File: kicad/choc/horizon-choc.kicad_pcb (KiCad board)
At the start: 2 copper layers, 252 x 68 mm, 115 parts, among them SW1 SW_Push, SW10 SW_Push, SW11 SW_Push, SW12 SW_Push, SW13 SW_Push, SW14 SW_Push, SW15 SW_Push, SW16 SW_Push, SW17 SW_Push, SW18 SW_Push, SW19 SW_Push, SW2 SW_Push, SW20 SW_Push, SW21 SW_Push, SW22 SW_Push, SW23 SW_Push, SW24 SW_Push, SW25 SW_Push, SW26 SW_Push, SW27 SW_Push, SW28 SW_Push, SW29 SW_Push, SW3 SW_Push, SW30 SW_Push, SW31 SW_Push, SW32 SW_Push, SW33 SW_Push, SW34 SW_Push, SW35 SW_Push, SW36 SW_Push, SW37 SW_Push, SW38 SW_Push, SW39 SW_Push, SW4 SW_Push, SW40 SW_Push, SW41 SW_Push, SW42 SW_Push, SW43 SW_Push, SW44 SW_Push, SW45 SW_Push, SW46 SW_Push, SW47 SW_Push, SW48 SW_Push, SW49 SW_Push, SW5 SW_Push, SW50 SW_Push, SW51 SW_Push, SW52 SW_Push, SW6 SW_Push, SW7 SW_Push, SW8 SW_Push, SW9 SW_Push, U1 PRO-MICRO

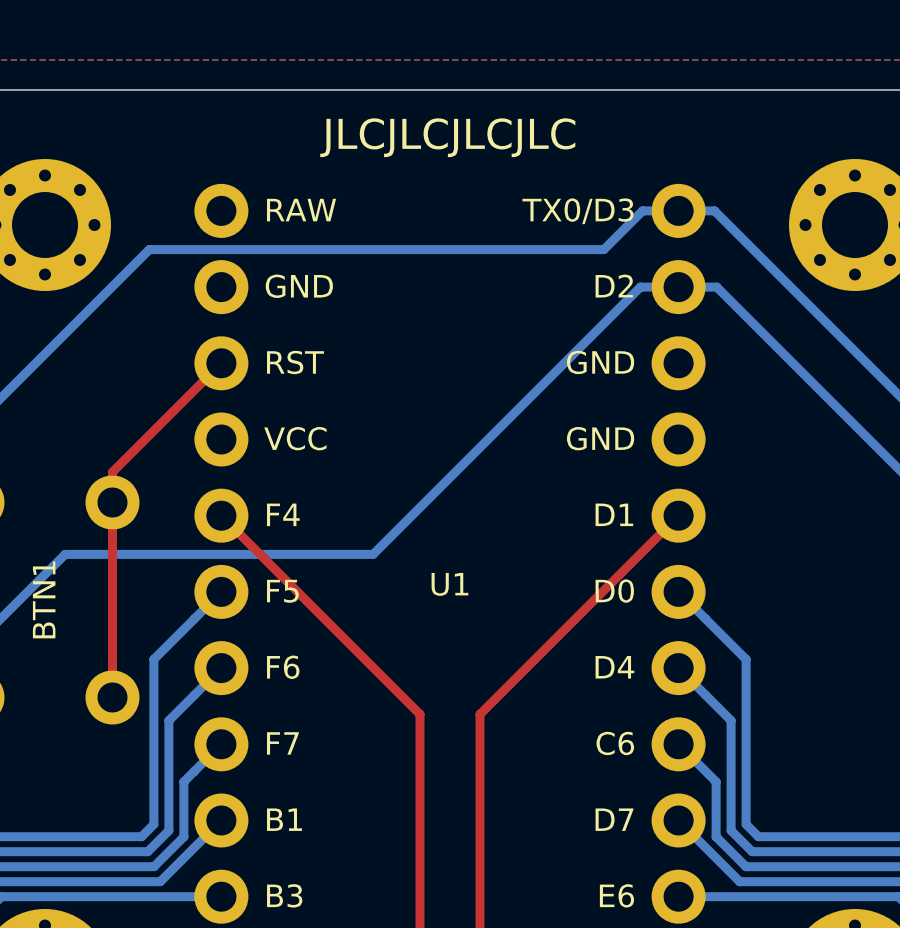
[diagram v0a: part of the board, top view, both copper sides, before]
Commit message: Preserve logos on plate PCBs
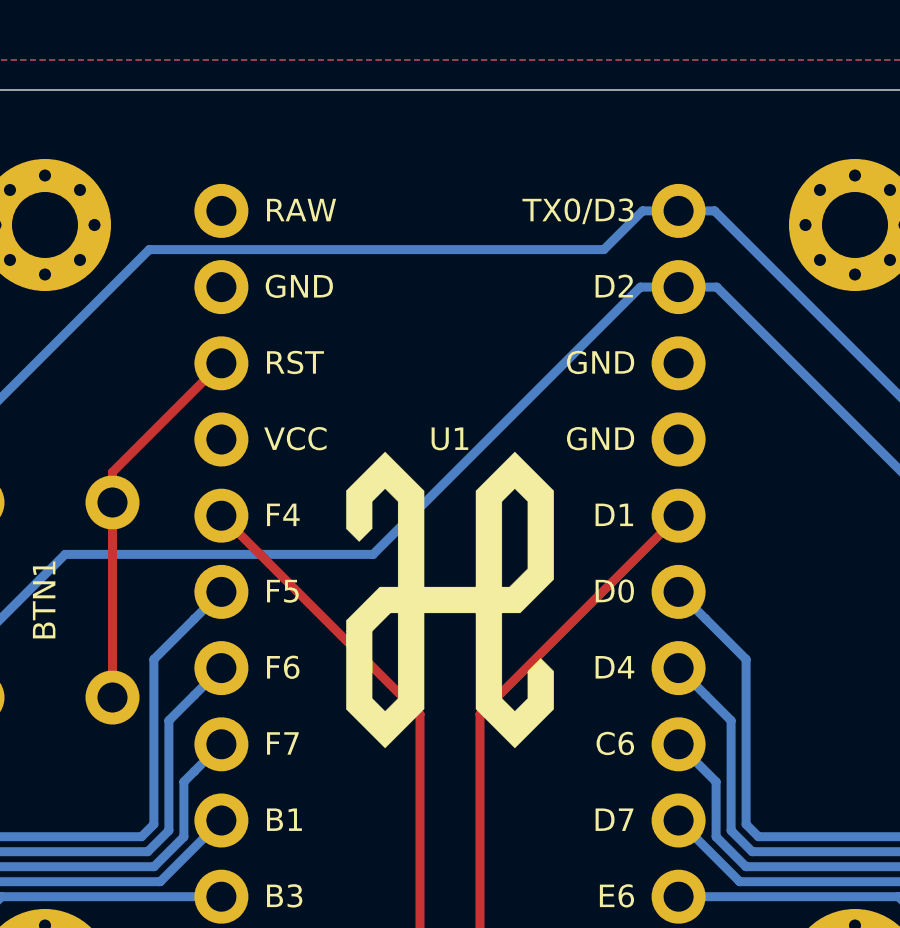
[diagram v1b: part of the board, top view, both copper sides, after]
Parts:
- added LOGO2: Logo-Top, horizon-footprints:Logo_Horizon_H, F.Cu at (202.0, 112.0)
- LOGO1: value Logo -> Logo-Bottom
- moved LOGO1 23.0 mm to (202.0, 100.5)
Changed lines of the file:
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@@
     (tracks 518)
     (zones 0)
-    (modules 115)
+    (modules 116)
     (nets 81)
   )
@@
     (add_net "Net-(H7-Pad1)")
     (add_net "Net-(H8-Pad1)")
+    (add_net "Net-(U1-Pad24)")
     (add_net RESET)
     (add_net ROW1)
@@
     (add_net ROW3)
     (add_net ROW4)
+    (add_net VCC)
   )
   (net_class Power ""
@@
     (add_net GND)
   )
+  (module horizon-footprints:Logo_Horizon_H (layer F.Cu)
+    (at 202 112)
+    (fp_text reference LOGO2 (at 0 2) (layer F.SilkS) hide
+      (effects (font (size 1.524 1.524) (thickness 0.3)))
+    )
+    (fp_text value Logo-Top (at 0 -2) (layer F.SilkS) hide
+      (effects (font (size 1.524 1.524) (thickness 0.3)))
+    )
+    (fp_poly (pts (xy 2.811161 -4.287795) (xy 3.459892 -3.639066) (xy 3.459892 -0.685799) (xy 2.900748 -0.126656)
+      (xy 2.341604 0.432486) (xy 1.731319 0.432486) (xy 1.731319 3.280722) (xy 1.94722 3.49662)
+      (xy 2.163122 3.712519) (xy 2.37902 3.496617) (xy 2.594919 3.280715) (xy 2.594919 2.378679)
+      (xy 2.810817 2.162777) (xy 2.83116 2.14244) (xy 2.850995 2.122623) (xy 2.870235 2.103411)
+      (xy 2.888793 2.084893) (xy 2.906579 2.067156) (xy 2.923508 2.050287) (xy 2.93949 2.034374)
+      (xy 2.954438 2.019503) (xy 2.968264 2.005761) (xy 2.980881 1.993237) (xy 2.9922 1.982017)
+      (xy 3.002134 1.972189) (xy 3.010594 1.96384) (xy 3.017494 1.957056) (xy 3.022745 1.951926)
+      (xy 3.02626 1.948537) (xy 3.02795 1.946975) (xy 3.028092 1.946875) (xy 3.029178 1.947832)
+      (xy 3.032118 1.950645) (xy 3.036821 1.955226) (xy 3.043201 1.961488) (xy 3.051169 1.969343)
+      (xy 3.060638 1.978705) (xy 3.07152 1.989485) (xy 3.083726 2.001596) (xy 3.097169 2.014952)
+      (xy 3.111761 2.029464) (xy 3.127413 2.045045) (xy 3.144038 2.061608) (xy 3.161548 2.079065)
+      (xy 3.179855 2.097329) (xy 3.198872 2.116313) (xy 3.218509 2.135929) (xy 3.238679 2.15609)
+      (xy 3.24468 2.162091) (xy 3.459892 2.377306) (xy 3.459892 3.639066) (xy 2.16243 4.936524)
+      (xy 1.513702 4.287791) (xy 0.864973 3.639058) (xy 0.864973 0.432486) (xy -0.8636 0.432486)
+      (xy -0.8636 3.639058) (xy -1.511985 4.287448) (xy -1.547393 4.322855) (xy -1.582321 4.357781)
+      (xy -1.616719 4.392174) (xy -1.650537 4.425985) (xy -1.683724 4.459163) (xy -1.716229 4.491659)
+      (xy -1.748003 4.52342) (xy -1.778995 4.554399) (xy -1.809155 4.584543) (xy -1.838431 4.613803)
+      (xy -1.866775 4.642128) (xy -1.894136 4.669469) (xy -1.920462 4.695774) (xy -1.945705 4.720994)
+      (xy -1.969813 4.745078) (xy -1.992736 4.767976) (xy -2.014425 4.789637) (xy -2.034827 4.810012)
+      (xy -2.053894 4.82905) (xy -2.071574 4.8467) (xy -2.087818 4.862913) (xy -2.102575 4.877638)
+      (xy -2.115795 4.890825) (xy -2.127427 4.902423) (xy -2.13742 4.912383) (xy -2.145726 4.920653)
+      (xy -2.152293 4.927184) (xy -2.15707 4.931925) (xy -2.160008 4.934826) (xy -2.161057 4.935837)
+      (xy -2.161058 4.935838) (xy -2.162058 4.934875) (xy -2.16495 4.932021) (xy -2.169682 4.927325)
+      (xy -2.176204 4.920839) (xy -2.184467 4.912612) (xy -2.194419 4.902694) (xy -2.20601 4.891136)
+      (xy -2.21919 4.877989) (xy -2.233909 4.863302) (xy -2.250116 4.847126) (xy -2.267761 4.829511)
+      (xy -2.286794 4.810508) (xy -2.307164 4.790166) (xy -2.32882 4.768536) (xy -2.351713 4.745669)
+      (xy -2.375792 4.721614) (xy -2.401007 4.696422) (xy -2.427307 4.670144) (xy -2.454642 4.642829)
+      (xy -2.482962 4.614527) (xy -2.512216 4.585291) (xy -2.542354 4.555168) (xy -2.573326 4.52421)
+      (xy -2.605081 4.492468) (xy -2.637569 4.45999) (xy -2.670739 4.426829) (xy -2.704541 4.393033)
+      (xy -2.738926 4.358654) (xy -2.773842 4.323741) (xy -2.810133 4.28745) (xy -3.458519 3.639063)
+      (xy -3.458519 1.044143) (xy -2.593546 1.044143) (xy -2.593546 3.280715) (xy -2.377648 3.496617)
+      (xy -2.161749 3.712519) (xy -1.945848 3.49662) (xy -1.729946 3.280722) (xy -1.729946 0.432486)
+      (xy -1.981884 0.432486) (xy -2.287715 0.738315) (xy -2.593546 1.044143) (xy -3.458519 1.044143)
+      (xy -3.458519 0.685798) (xy -2.899375 0.126656) (xy -2.340231 -0.432487) (xy -1.729946 -0.432487)
+      (xy -1.729946 -3.280722) (xy -1.945848 -3.496621) (xy -2.161749 -3.712519) (xy -2.377648 -3.496618)
+      (xy -2.593546 -3.280716) (xy -2.593546 -2.378679) (xy -2.809445 -2.162778) (xy -2.829787 -2.142441)
+      (xy -2.849622 -2.122623) (xy -2.868863 -2.103412) (xy -2.88742 -2.084894) (xy -2.905207 -2.067157)
+      (xy -2.922135 -2.050288) (xy -2.938117 -2.034374) (xy -2.953065 -2.019503) (xy -2.966892 -2.005762)
+      (xy -2.979508 -1.993238) (xy -2.990827 -1.982018) (xy -3.000761 -1.97219) (xy -3.009222 -1.96384)
+      (xy -3.016122 -1.957057) (xy -3.021373 -1.951927) (xy -3.024887 -1.948537) (xy -3.026578 -1.946975)
+      (xy -3.026719 -1.946876) (xy -3.027806 -1.947833) (xy -3.030745 -1.950646) (xy -3.035449 -1.955227)
+      (xy -3.041829 -1.961488) (xy -3.049797 -1.969344) (xy -3.059266 -1.978705) (xy -3.070147 -1.989485)
+      (xy -3.082354 -2.001597) (xy -3.095797 -2.014952) (xy -3.110388 -2.029464) (xy -3.126041 -2.045045)
+      (xy -3.142666 -2.061608) (xy -3.160176 -2.079066) (xy -3.178483 -2.09733) (xy -3.197499 -2.116314)
+      (xy -3.217136 -2.13593) (xy -3.237306 -2.156091) (xy -3.243307 -2.162091) (xy -3.458519 -2.377306)
+      (xy -3.458519 -3.639066) (xy -2.809789 -4.287795) (xy -2.161058 -4.936525) (xy -0.8636 -3.639059)
+      (xy -0.8636 -0.432487) (xy 0.864973 -0.432487) (xy 0.864973 -3.280716) (xy 1.731319 -3.280716)
+      (xy 1.731319 -0.432487) (xy 1.983257 -0.432487) (xy 2.289088 -0.738315) (xy 2.594919 -1.044144)
+      (xy 2.594919 -3.280722) (xy 2.379017 -3.496621) (xy 2.163115 -3.712519) (xy 1.947217 -3.496618)
+      (xy 1.731319 -3.280716) (xy 0.864973 -3.280716) (xy 0.864973 -3.639059) (xy 1.513702 -4.287792)
+      (xy 2.16243 -4.936525) (xy 2.811161 -4.287795)) (layer F.SilkS) (width 0.01))
+  )
   (module horizon-footprints:Logo_Horizon_Small (layer B.Cu)
-    (at 202 123.5 180)
-    (fp_text reference LOGO1 (at 0 0) (layer B.SilkS) hide
+    (at 202 100.5 180)
+    (fp_text reference LOGO1 (at 0 -2) (layer B.SilkS) hide
       (effects (font (size 1.524 1.524) (thickness 0.3)) (justify mirror))
     )
-    (fp_text value Logo (at 0.75 0) (layer B.SilkS) hide
+    (fp_text value Logo-Bottom (at -0.1 1) (layer B.SilkS) hide
       (effects (font (size 1.524 1.524) (thickness 0.3)) (justify mirror))
     )
@@
     (descr "SparkFun Arduino Pro Micro ATmega32U4")
     (tags "Arduino, Pro Micro")
-    (fp_text reference U1 (at 0 16.5) (layer F.SilkS)
+    (fp_text reference U1 (at 0 11.65) (layer F.SilkS)
       (effects (font (size 0.75 0.75) (thickness 0.15)))
     )
-    (fp_text value PRO-MICRO (at 0 18) (layer F.SilkS) hide
+    (fp_text value PRO-MICRO (at 0 13.65) (layer F.SilkS) hide
       (effects (font (size 0.75 0.75) (thickness 0.15)))
     )
@@
   (gr_line (start 328 161) (end 328 97) (layer B.Adhes) (width 0.05))
   (gr_line (start 78 163) (end 326 163) (layer B.Adhes) (width 0.05))
-  (gr_text "rev2 | Choc" (at 202 127.5) (layer B.SilkS)
+  (gr_text "rev2 | Choc" (at 202 104.5) (layer B.SilkS)
     (effects (font (size 1 1) (thickness 0.15)) (justify mirror))
   )
@@
   (gr_arc (start 326 161) (end 326 163) (angle -90) (layer Edge.Cuts) (width 0.05))
   (gr_line (start 328 97) (end 328 161) (layer Edge.Cuts) (width 0.05))
-  (gr_text JLCJLCJLCJLC (at 202 96.5) (layer F.SilkS)
-    (effects (font (size 1 1) (thickness 0.15)))
+  (gr_text JLCJLCJLCJLC (at 202 106.5) (layer B.SilkS)
+    (effects (font (size 1 1) (thickness 0.15)) (justify mirror))
   )
-  (gr_text github.com/skarrmann/horizon (at 202 129.5) (layer B.SilkS)
+  (gr_text github.com/skarrmann/horizon (at 202 96.5) (layer B.SilkS)
     (effects (font (size 1 1) (thickness 0.15)) (justify mirror))
   )

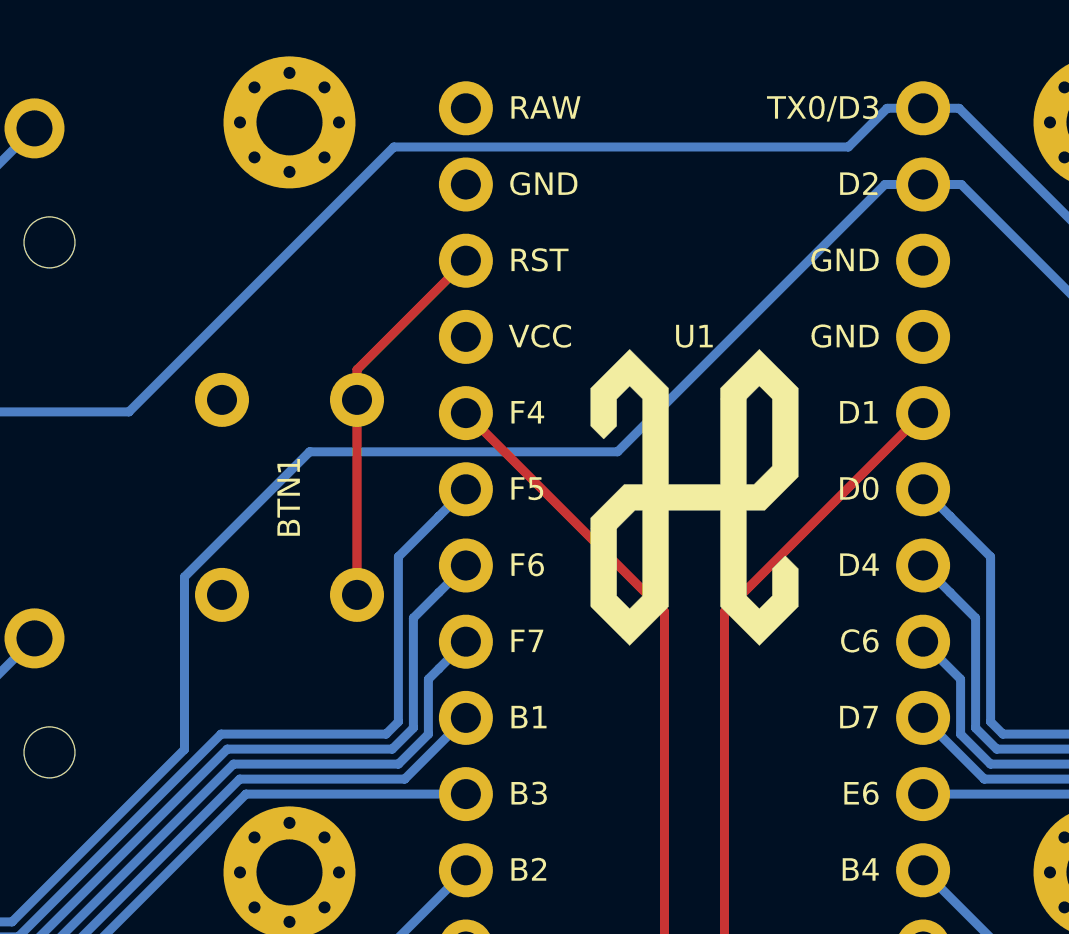
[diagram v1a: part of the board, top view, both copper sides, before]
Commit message: Remove unused footprints and other files. Update readme. Prepare for production!
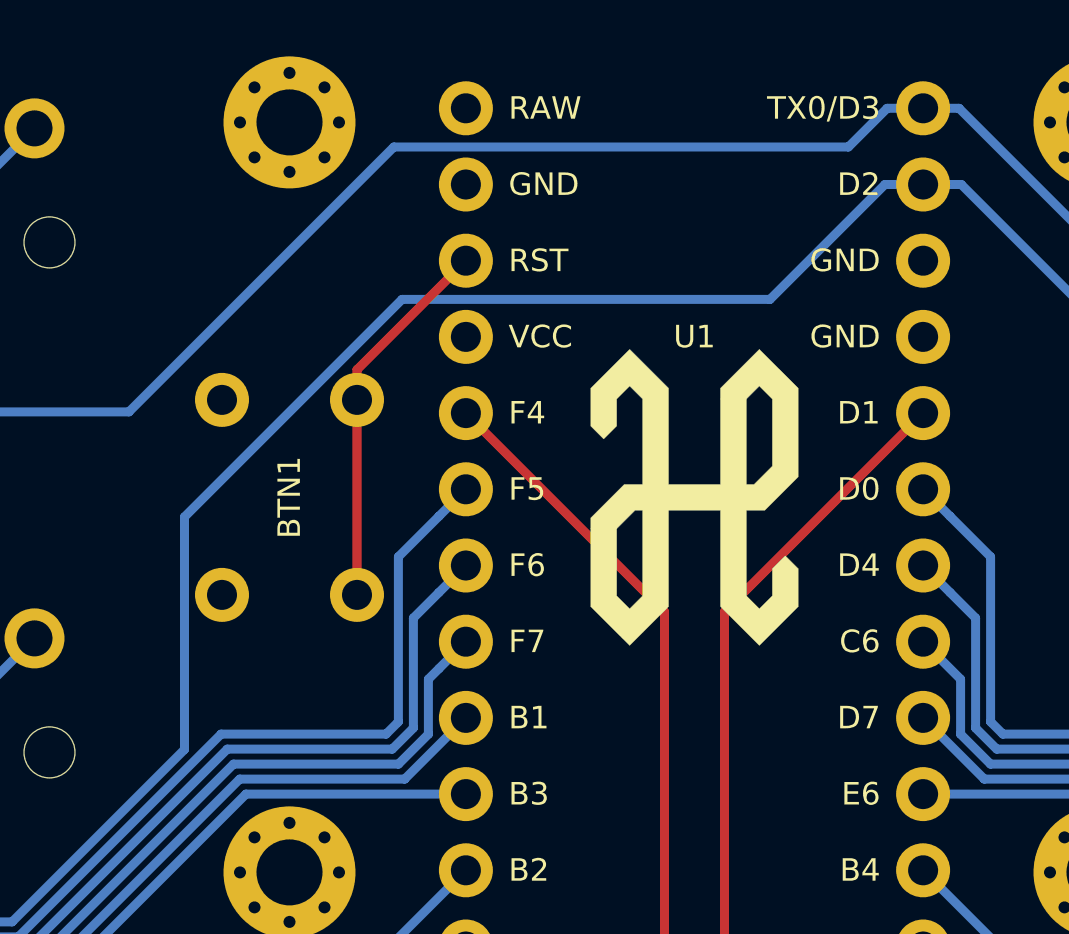
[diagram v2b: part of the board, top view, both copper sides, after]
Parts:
- moved LOGO1 11.0 mm to (202.0, 111.5)
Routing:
- net ROW2: track 285.7 -> 286.9 mm
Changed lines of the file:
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@@
     (add_net "Net-(H7-Pad1)")
     (add_net "Net-(H8-Pad1)")
-    (add_net "Net-(U1-Pad24)")
     (add_net RESET)
     (add_net ROW1)
@@
     (add_net ROW3)
     (add_net ROW4)
-    (add_net VCC)
   )
   (net_class Power ""
@@
   )
   (module horizon-footprints:Logo_Horizon_Small (layer B.Cu)
-    (at 202 100.5 180)
+    (at 202 111.5 180)
     (fp_text reference LOGO1 (at 0 -2) (layer B.SilkS) hide
       (effects (font (size 1.524 1.524) (thickness 0.3)) (justify mirror))
@@
   (gr_line (start 328 161) (end 328 97) (layer B.Adhes) (width 0.05))
   (gr_line (start 78 163) (end 326 163) (layer B.Adhes) (width 0.05))
-  (gr_text "rev2 | Choc" (at 202 104.5) (layer B.SilkS)
+  (gr_text "rev2 | Choc" (at 202 115.5) (layer B.SilkS)
     (effects (font (size 1 1) (thickness 0.15)) (justify mirror))
   )
@@
   (gr_arc (start 326 161) (end 326 163) (angle -90) (layer Edge.Cuts) (width 0.05))
   (gr_line (start 328 97) (end 328 161) (layer Edge.Cuts) (width 0.05))
-  (gr_text JLCJLCJLCJLC (at 202 106.5) (layer B.SilkS)
+  (gr_text JLCJLCJLCJLC (at 202 127.5) (layer B.SilkS)
     (effects (font (size 1 1) (thickness 0.15)) (justify mirror))
   )
@@
   (segment (start 225.649999 126.150001) (end 315.649999 126.150001) (width 0.3) (layer B.Cu) (net 51))
   (segment (start 225.649999 126.150001) (end 226.6 125.2) (width 0.3) (layer B.Cu) (net 51))
-  (segment (start 84.1 125.2) (end 83.35 125.2) (width 0.3) (layer B.Cu) (net 51))
-  (segment (start 209.62 101.57) (end 208.347208 101.57) (width 0.3) (layer B.Cu) (net 51))
-  (segment (start 208.347208 101.57) (end 199.437209 110.479999) (width 0.3) (layer B.Cu) (net 51))
-  (segment (start 199.437209 110.479999) (end 189.169999 110.479999) (width 0.3) (layer B.Cu) (net 51))
-  (segment (start 189.169999 110.479999) (end 184.999999 114.649999) (width 0.3) (layer B.Cu) (net 51))
-  (segment (start 184.999999 114.649999) (end 184.999999 120.402881) (width 0.3) (layer B.Cu) (net 51))
-  (segment (start 85.050001 126.150001) (end 84.1 125.2) (width 0.3) (layer B.Cu) (net 51))
-  (segment (start 179.252879 126.150001) (end 85.050001 126.150001) (width 0.3) (layer B.Cu) (net 51))
-  (segment (start 184.999999 120.402881) (end 179.252879 126.150001) (width 0.3) (layer B.Cu) (net 51))
   (segment (start 224.747121 126.150001) (end 225.649999 126.150001) (width 0.3) (layer B.Cu) (net 51))
   (segment (start 218.550001 119.952881) (end 224.747121 126.150001) (width 0.3) (layer B.Cu) (net 51))
@@
   (segment (start 210.892792 101.57) (end 218.550001 109.227209) (width 0.3) (layer B.Cu) (net 51))
   (segment (start 209.62 101.57) (end 210.892792 101.57) (width 0.3) (layer B.Cu) (net 51))
+  (segment (start 85.050001 126.150001) (end 84.1 125.2) (width 0.3) (layer B.Cu) (net 51))
+  (segment (start 84.1 125.2) (end 83.35 125.2) (width 0.3) (layer B.Cu) (net 51))
+  (segment (start 179.252879 126.150001) (end 85.050001 126.150001) (width 0.3) (layer B.Cu) (net 51))
+  (segment (start 209.62 101.57) (end 208.347208 101.57) (width 0.3) (layer B.Cu) (net 51))
+  (segment (start 208.347208 101.57) (end 204.517209 105.399999) (width 0.3) (layer B.Cu) (net 51))
+  (segment (start 204.517209 105.399999) (end 192.249999 105.399999) (width 0.3) (layer B.Cu) (net 51))
+  (segment (start 192.249999 105.399999) (end 184.999999 112.649999) (width 0.3) (layer B.Cu) (net 51))
+  (segment (start 184.999999 112.649999) (end 184.999999 120.402881) (width 0.3) (layer B.Cu) (net 51))
+  (segment (start 184.999999 120.402881) (end 179.252879 126.150001) (width 0.3) (layer B.Cu) (net 51))
   (segment (start 243.649999 143.150001) (end 244.6 142.2) (width 0.3) (layer B.Cu) (net 52))
   (segment (start 189.649999 143.150001) (end 190.6 142.2) (width 0.3) (layer B.Cu) (net 52))
